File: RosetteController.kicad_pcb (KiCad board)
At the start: 4 copper layers, 100 x 50 mm, 10 parts

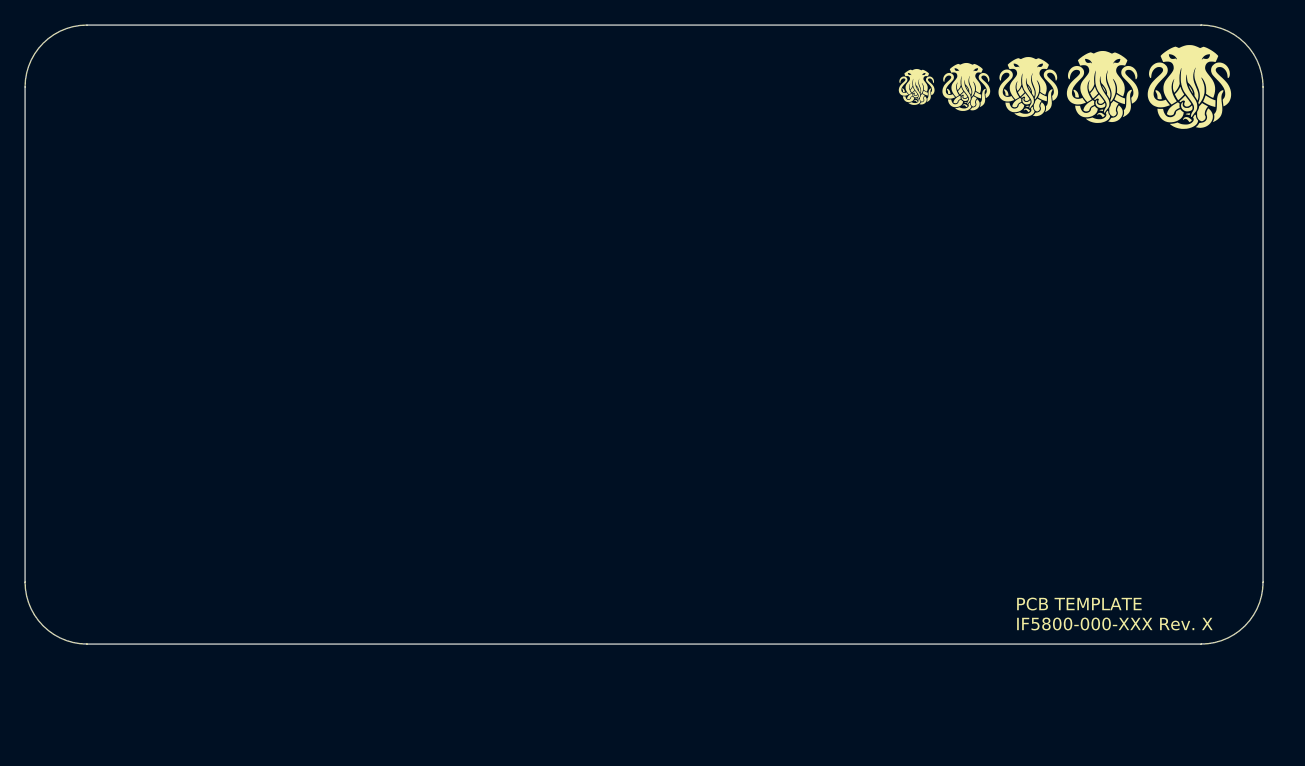
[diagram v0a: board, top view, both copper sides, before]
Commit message: Increased capacitance on motor driver
Increased capacitance on motor driver from 4.7uF to 44uF based on evaluation board testing.
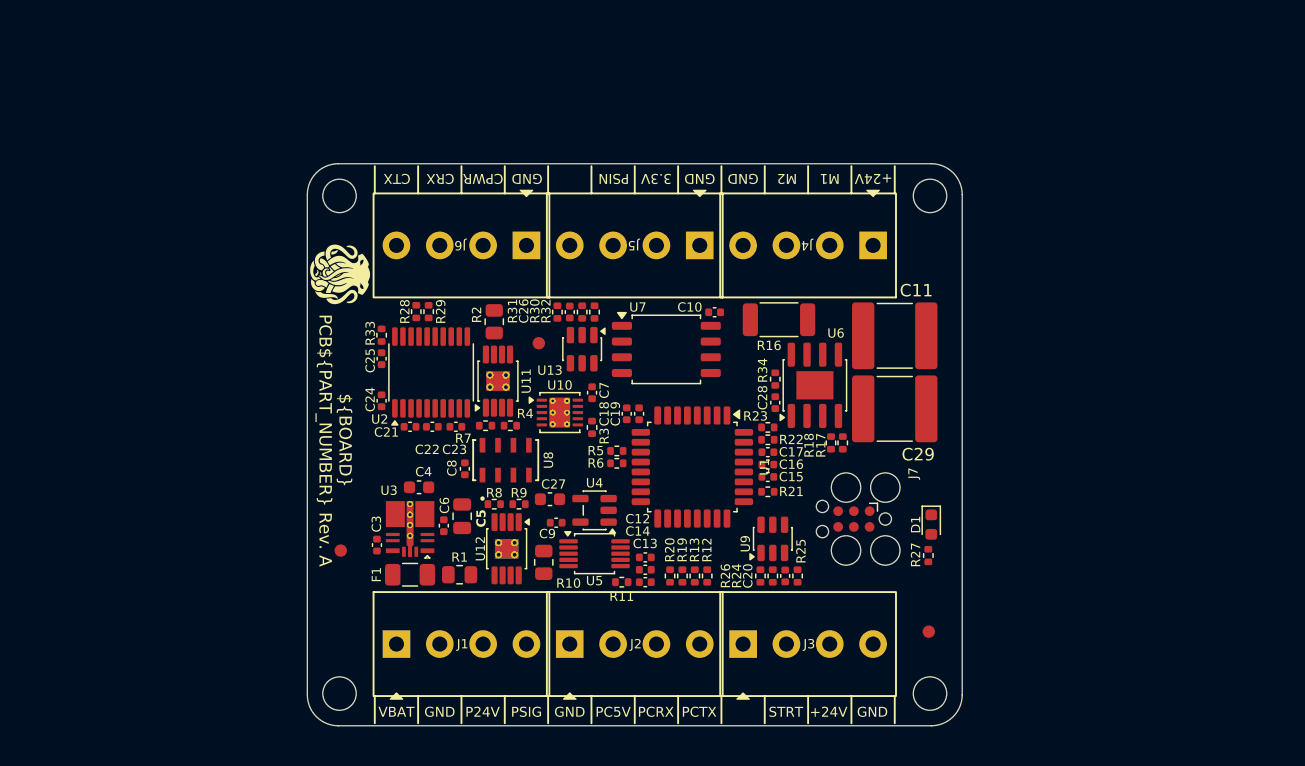
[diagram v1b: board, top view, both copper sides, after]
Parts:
- removed the G*** at (222.0, 105.0)
- removed the G*** at (174.0, 144.0)
- removed the G*** at (237.0, 105.0)
- removed the G*** at (226.0, 105.0)
- removed the G*** at (244.0, 105.0)
- removed the G*** at (169.0, 144.0)
- removed the G*** at (163.0, 144.0)
- removed the G*** at (178.0, 144.0)
- removed the G*** at (156.0, 144.0)
- added ?: , , F.Cu at (191.5, 125.7)
- added ?: , , F.Cu at (175.5, 142.4)
- added ?: Fiducial_1mm_Mask3mm, Fiducial:Fiducial_1mm_Mask3mm, F.Cu at (223.0, 149.0)
- added C10: 100nF, Capacitor_SMD:C_0402_1005Metric, F.Cu at (205.7, 123.2)
- added C11: 22uF, Capacitor_SMD:C_2220_5750Metric, F.Cu at (220.2, 125.1)
- added C12: 100nF, Capacitor_SMD:C_0402_1005Metric, F.Cu at (200.1, 143.0)
- added C13: 1uF, Capacitor_SMD:C_0402_1005Metric, F.Cu at (200.1, 145.0)
- added C14: 100nF, Capacitor_SMD:C_0402_1005Metric, F.Cu at (200.1, 144.0)
- added C15: 1uF, Capacitor_SMD:C_0402_1005Metric, F.Cu at (210.0, 136.5)
- added C16: 100nF, Capacitor_SMD:C_0402_1005Metric, F.Cu at (210.0, 135.5)
- added C17: 100nF, Capacitor_SMD:C_0402_1005Metric, F.Cu at (210.0, 134.5)
- added C18: 1uF, Capacitor_SMD:C_0402_1005Metric, F.Cu at (198.6, 131.4)
- added C19: 100nF, Capacitor_SMD:C_0402_1005Metric, F.Cu at (199.6, 131.4)
- added C20: 100nF, Capacitor_SMD:C_0402_1005Metric, F.Cu at (211.4, 144.5)
- added C21: 100nF, Capacitor_SMD:C_0402_1005Metric, F.Cu at (181.1, 132.4)
- added C22: 100nF, Capacitor_SMD:C_0402_1005Metric, F.Cu at (182.9, 132.4)
- added C23: 100nF, Capacitor_SMD:C_0402_1005Metric, F.Cu at (184.8, 132.4)
- added C24: 100nF, Capacitor_SMD:C_0402_1005Metric, F.Cu at (178.8, 130.3)
- added C25: 100nF, Capacitor_SMD:C_0402_1005Metric, F.Cu at (178.8, 126.9)
- added C26: 100nF, Capacitor_SMD:C_0402_1005Metric, F.Cu at (194.0, 123.2)
- added C27: 22uF, Capacitor_SMD:C_0603_1608Metric, F.Cu at (192.4, 138.3)
- added C28: 100nF, Capacitor_SMD:C_0402_1005Metric, F.Cu at (210.6, 130.5)
- added C29: 22uF, Capacitor_SMD:C_2220_5750Metric, F.Cu at (220.2, 131.0)
- added C3: 1uF, Capacitor_SMD:C_0402_1005Metric, F.Cu at (178.4, 142.0)
- added C4: 22uF, Capacitor_SMD:C_0603_1608Metric, F.Cu at (181.8, 137.3)
- added C5: 4.7uF, Capacitor_SMD:C_0805_2012Metric, F.Cu at (185.3, 139.7)
- added C6: 100nF, Capacitor_SMD:C_0402_1005Metric, F.Cu at (183.8, 140.4)
- added C7: 100nF, Capacitor_SMD:C_0402_1005Metric, F.Cu at (195.8, 129.7)
- added C8: 100nF, Capacitor_SMD:C_0402_1005Metric, F.Cu at (185.5, 135.8)
- added C9: 1uF, Capacitor_SMD:C_0402_1005Metric, F.Cu at (192.9, 140.2)
- added D1: LTST-C191KRKT, LED_SMD:LED_0603_1608Metric, F.Cu at (223.2, 140.3)
- added F1: 5A, Fuse:Fuse_1206_3216Metric, F.Cu at (181.1, 144.4)
- added J1: 284391-4, prj-footprints:CONN4_284391-4_TEC, F.Cu at (180.0, 150.0)
- added J2: 284391-4, prj-footprints:CONN4_284391-4_TEC, F.Cu at (194.0, 150.0)
- added J3: 284391-4, prj-footprints:CONN4_284391-4_TEC, F.Cu at (208.0, 150.0)
- added J4: 284391-4, prj-footprints:CONN4_284391-4_TEC, F.Cu at (218.5, 117.8)
- added J5: 284391-4, prj-footprints:CONN4_284391-4_TEC, F.Cu at (204.5, 117.8)
- added J6: 284391-4, prj-footprints:CONN4_284391-4_TEC, F.Cu at (190.5, 117.8)
- added J7: Conn_ARM_SWD_TagConnect_TC2030, Connector:Tag-Connect_TC2030-IDC-FP_2x03_P1.27mm_Vertical, F.Cu at (216.9, 139.9)
- added R1: 10m, Resistor_SMD:R_0805_2012Metric, F.Cu at (185.1, 144.4)
- added R10: 120, Resistor_SMD:R_0805_2012Metric, F.Cu at (191.9, 143.4)
- added R11: 0, Resistor_SMD:R_0402_1005Metric, F.Cu at (198.2, 145.0)
- added R12: 1k, Resistor_SMD:R_0402_1005Metric, F.Cu at (205.1, 144.5)
- added R13: 1k, Resistor_SMD:R_0402_1005Metric, F.Cu at (204.1, 144.5)
- added R16: 100m, Resistor_SMD:R_2010_5025Metric, F.Cu at (210.9, 123.8)
- added R17: 10k, Resistor_SMD:R_0402_1005Metric, F.Cu at (216.1, 133.8)
- added R18: 10k, Resistor_SMD:R_0402_1005Metric, F.Cu at (215.1, 133.8)
- added R19: 10k, Resistor_SMD:R_0402_1005Metric, F.Cu at (203.1, 144.5)
- added R2: 10m, Resistor_SMD:R_0805_2012Metric, F.Cu at (187.9, 124.0)
- added R20: 5k, Resistor_SMD:R_0402_1005Metric, F.Cu at (202.1, 144.5)
- added R21: 10k, Resistor_SMD:R_0402_1005Metric, F.Cu at (210.0, 137.7)
- added R22: 10k, Resistor_SMD:R_0402_1005Metric, F.Cu at (210.0, 133.5)
- added R23: 10k, Resistor_SMD:R_0402_1005Metric, F.Cu at (210.0, 132.5)
- added R24: 100k, Resistor_SMD:R_0402_1005Metric, F.Cu at (210.4, 144.5)
- added R25: 10k, Resistor_SMD:R_0402_1005Metric, F.Cu at (212.4, 144.5)
- added R26: 10k, Resistor_SMD:R_0402_1005Metric, F.Cu at (209.4, 144.5)
- added R27: 330, Resistor_SMD:R_0402_1005Metric, F.Cu at (223.0, 142.8)
- added R28: 330, Resistor_SMD:R_0402_1005Metric, F.Cu at (181.6, 123.1)
- added R29: 330, Resistor_SMD:R_0402_1005Metric, F.Cu at (182.6, 123.1)
- added R3: 10k, Resistor_SMD:R_0402_1005Metric, F.Cu at (195.8, 132.5)
- added R30: 10k, Resistor_SMD:R_0402_1005Metric, F.Cu at (195.0, 123.2)
- added R31: 10k, Resistor_SMD:R_0402_1005Metric, F.Cu at (193.0, 123.2)
- added R32: 10k, Resistor_SMD:R_0402_1005Metric, F.Cu at (196.0, 123.2)
- added R33: 100k, Resistor_SMD:R_0402_1005Metric, F.Cu at (178.8, 125.0)
- added R34: 10k, Resistor_SMD:R_0402_1005Metric, F.Cu at (210.6, 128.6)
- added R4: 1k, Resistor_SMD:R_0402_1005Metric, F.Cu at (189.2, 132.4)
- added R5: 10k, Resistor_SMD:R_0402_1005Metric, F.Cu at (197.8, 134.4)
- added R6: 10k, Resistor_SMD:R_0402_1005Metric, F.Cu at (197.8, 135.4)
- added R7: 10k, Resistor_SMD:R_0402_1005Metric, F.Cu at (187.2, 132.4)
- added R8: 1k, Resistor_SMD:R_0402_1005Metric, F.Cu at (187.9, 138.7)
- added R9: 10k, Resistor_SMD:R_0402_1005Metric, F.Cu at (189.9, 138.7)
- added REF**: MountingHole_2.7mm_M2.5_ISO14580, MountingHole:MountingHole_2.7mm_M2.5_ISO14580, F.Cu at (175.4, 154.0)
- added REF**: MountingHole_2.7mm_M2.5_ISO14580, MountingHole:MountingHole_2.7mm_M2.5_ISO14580, F.Cu at (175.4, 113.8)
- added REF**: MountingHole_2.7mm_M2.5_ISO14580, MountingHole:MountingHole_2.7mm_M2.5_ISO14580, F.Cu at (223.1, 154.0)
- added REF**: MountingHole_2.7mm_M2.5_ISO14580, MountingHole:MountingHole_2.7mm_M2.5_ISO14580, F.Cu at (223.1, 113.8)
- added U1: PIC32CM1216MC00032, Package_QFP:TQFP-32_7x7mm_P0.8mm, F.Cu at (203.9, 135.7)
- added U10: PAC1720, Package_DFN_QFN:DFN-10-1EP_3x3mm_P0.5mm_EP1.65x2.38mm_ThermalVias, F.Cu at (193.2, 131.3)
- added U11: TPS1H000, Package_SO:HVSSOP-8-1EP_3x3mm_P0.65mm_EP1.57x1.89mm_ThermalVias, F.Cu at (188.2, 128.8)
- added U12: TPS1H000, Package_SO:HVSSOP-8-1EP_3x3mm_P0.65mm_EP1.57x1.89mm_ThermalVias, F.Cu at (188.9, 142.3)
- added U13: TLV6713, Package_TO_SOT_SMD:TSOT-23-6, F.Cu at (195.0, 126.2)
- added U2: MAX3222EIPWR, Package_SO:Texas_PW0020A_TSSOP-20_4.4x6.5mm_P0.65mm, F.Cu at (182.8, 128.1)
- added U3: TPSM33610S3Q, Inkfish_IC:U_QFN-FCMOD_RDN0011B_TEX, F.Cu at (181.1, 140.5)
- added U4: LM4132AMF-2.0, Package_TO_SOT_SMD:SOT-23-5, F.Cu at (196.0, 139.2)
- added U5: MAX11201, Package_SO:MSOP-10_3x3mm_P0.5mm, F.Cu at (196.0, 142.7)
- added U6: TB67H450AFNG, Package_SO:SOIC-8-1EP_3.9x4.9mm_P1.27mm_EP2.29x3mm, F.Cu at (213.8, 129.1)
- added U7: MX25L25645G, Package_SO:SOIC-8_5.3x5.3mm_P1.27mm, F.Cu at (201.8, 126.2)
- added U8: MS860702BA01-50, Inkfish_Sensor:MS860702BA01-50_TEC, F.Cu at (188.8, 135.1)
- added U9: TLV6713, Package_TO_SOT_SMD:TSOT-23-6, F.Cu at (210.4, 141.5)
- moved G*** 57.6 mm to (175.4, 120.1), turned to -90 degrees
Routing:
- added copper zone on In2.Cu, net +3.3V
- added copper zone on In1.Cu, net GND
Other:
- board size 100 x 50 mm -> 52.9 x 45.4 mm
- board text added: "${BOARD} PCB${PART_NUMBER} Rev. ${REVISION}"
- board text added: "+24V"
- board text added: "3.3V"
- board text added: "CPWR"
- board text added: "CRX"
- board text added: "CTX"
- board text added: "GND"
- board text added: "M1"
- board text added: "M2"
- board text added: "P24V"
- board text added: "PC5V"
- board text added: "PCRX"
- board text added: "PCTX"
- board text added: "PSIG"
- board text added: "PSIN"
- board text added: "STRT"
- board text added: "VBAT"
- board text removed: "PCB TEMPLATE IF5800-000-XXX Rev. X"

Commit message: Layout Complete
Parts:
- removed ? (x2): , 
- removed J5, J6: 284391-4, prj-footprints:CONN4_284391-4_TEC
- removed R13: 1k, Resistor_SMD:R_0402_1005Metric
- added D2: PMEG60T50ELPX, Diode_SMD:D_SOD-128, F.Cu at (184.2, 140.3)
- added FID2: Fiducial_1mm_Mask3mm, Fiducial:Fiducial_1mm_Mask3mm, F.Cu at (172.3, 143.0)
- added FID3: Fiducial_1mm_Mask3mm, Fiducial:Fiducial_1mm_Mask3mm, F.Cu at (200.0, 127.0)
- added R35: 330, Resistor_SMD:R_0402_1005Metric, F.Cu at (193.3, 138.1)
- added R36: 330, Resistor_SMD:R_0402_1005Metric, F.Cu at (194.3, 138.1)
- added R37: DNP, Resistor_SMD:R_0402_1005Metric, F.Cu at (182.2, 144.0)
- added REF**: MountingHole_2.7mm_M2.5, MountingHole:MountingHole_2.7mm_M2.5, F.Cu at (172.3, 118.0)
- J1: value 284391-4 -> 0395016004; footprint prj-footprints:CONN4_284391-4_TEC -> Connector_Phoenix_MC:PhoenixContact_MCV_1,5_4-G-3.5_1x04_P3.50mm_Vertical
- J2: value 284391-4 -> 0395016008; footprint prj-footprints:CONN4_284391-4_TEC -> Connector_Phoenix_MC:PhoenixContact_MCV_1,5_8-G-3.5_1x08_P3.50mm_Vertical
- J3: value 284391-4 -> 0395016005; footprint prj-footprints:CONN4_284391-4_TEC -> Connector_Phoenix_MC:PhoenixContact_MCV_1,5_5-G-3.5_1x05_P3.50mm_Vertical
- J4: value 284391-4 -> 0395016006; footprint prj-footprints:CONN4_284391-4_TEC -> Connector_Phoenix_MC:PhoenixContact_MCV_1,5_6-G-3.5_1x06_P3.50mm_Vertical
- J7: footprint Connector:Tag-Connect_TC2030-IDC-FP_2x03_P1.27mm_Vertical -> Connector:Tag-Connect_TC2030-IDC-NL_2x03_P1.27mm_Vertical
- R12: value 1k -> 0
- REF** (x4): value MountingHole_2.7mm_M2.5_ISO14580 -> MountingHole_2.7mm_M2.5; footprint MountingHole:MountingHole_2.7mm_M2.5_ISO14580 -> MountingHole:MountingHole_2.7mm_M2.5
- moved REF** 55.0 mm to (172.3, 135.0)
- moved G*** 50.3 mm to (225.6, 125.0), turned to 90 degrees
- moved REF** 50.1 mm to (225.3, 118.0)
- moved J3 33.5 mm to (217.4, 117.9), turned to 180 degrees
- moved R12 23.0 mm to (182.2, 142.1), turned to -90 degrees
- moved J4 21.0 mm to (197.5, 117.9)
- moved C10 19.2 mm to (214.5, 140.3), turned to 90 degrees
- moved C7 16.7 mm to (179.7, 134.3), turned to -90 degrees
- moved R3 16.1 mm to (179.7, 131.5), turned to -90 degrees
- moved U7 15.0 mm to (211.1, 137.9), turned to -90 degrees
- moved R23 12.6 mm to (206.4, 144.6), turned to 90 degrees
- moved R21 12.2 mm to (199.9, 144.6), turned to 90 degrees
- moved R22 11.9 mm to (205.5, 144.6), turned to 90 degrees
- moved C17 11.4 mm to (204.6, 144.6), turned to -90 degrees
- moved R7 11.1 mm to (196.8, 126.7), turned to 90 degrees
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- gave numbers to parts that had none: 1
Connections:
- F1 pad 2: Net-(U10-SENSE1+) -> Net-(D2-A)
- J1 pad 1: /VBATT+ -> GND
- J1 pad 2: GND -> /VBATT+
- J2 pad 3: /FTDI_RX -> /RS232_RX
- J2 pad 4: /FTDI_TX -> /RS232_TX
- J3 pad 1: unconnected-(J3-Pin_1-Pad1) -> GND
- J3 pad 2: /START_PLUG -> /MOTOR1
- J3 pad 3: +24V -> /MOTOR2
- J3 pad 4: GND -> +3.3V
- J4 pad 1: +24V -> GND
- J4 pad 2: /MOTOR1 -> /CTD_PWR
- J4 pad 3: /MOTOR2 -> /CTD_RX
- J4 pad 4: GND -> /CTD_TX
- R1 pad 1: Net-(U10-SENSE1+) -> Net-(D2-K)
- R12 pad 1: /FTDI_TX -> +3.3V
- R12 pad 2: /PC_TXD -> Net-(U3-FB)
- U1 pad 1: /PRES_ON -> /RUN_WAKE
- U1 pad 14: /PAC_ALERT -> /HALL_SENSOR
- U1 pad 19: /HALL_SENSOR -> /PAC_ALERT
- U1 pad 20: /RUN_WAKE -> /RS232_SHDN
- U1 pad 23: /LED -> /PRES_ON
- U1 pad 4: /RS232_SHDN -> /LED
- U10 pad 1: Net-(U10-SENSE1+) -> Net-(D2-K)
- U2 pad 10: unconnected-(U2-ROUT2-Pad10) -> /PC_RXD
- U2 pad 12: GND -> /PC_TXD
- U2 pad 8: unconnected-(U2-DOUT2-Pad8) -> Net-(U2-DOUT2)
- U2 pad 9: GND -> Net-(U2-RIN2)
- U3 pad 9: +3.3V -> Net-(U3-FB)
- U6 pad 9: (no net) -> GND
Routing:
- net GND: track 0.00 -> 72.1 mm, vias 0 -> 69
- net +24V: track 0.00 -> 44.0 mm, vias 0 -> 21
- net /SDA: track 0.00 -> 41.7 mm, vias 0 -> 2
- net /SCL: track 0.00 -> 40.1 mm, vias 0 -> 2
- net +3.3V: track 0.00 -> 36.6 mm, vias 0 -> 25
- net /PAC_ALERT: track 0.00 -> 28.2 mm, vias 0 -> 2
- net /RS232_TX: track 0.00 -> 25.2 mm, vias 0 -> 2
- net /RS232_SHDN: track 0.00 -> 22.9 mm, vias 0 -> 2
- net /CTD_PWR: track 0.00 -> 20.7 mm
- net /CTD_ON: track 0.00 -> 20.4 mm
- net /RS232_RX: track 0.00 -> 19.7 mm, vias 0 -> 2
- net /RESET: track 0.00 -> 17.9 mm, vias 0 -> 2
- net /MOTOR_IN1: track 0.00 -> 15.7 mm, vias 0 -> 2
- net /MOTOR_IN2: track 0.00 -> 15.3 mm, vias 0 -> 2
- net /HALL_SENSOR: track 0.00 -> 14.8 mm
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- added copper zone on B.Cu, net +24V
- added copper zone on F.Cu, net +24V
- added copper zone on F.Cu, net +3.3V
- added copper zone on F.Cu, net /MOTOR1
- added copper zone on F.Cu, net /MOTOR2
- added copper zone on F.Cu, net GND
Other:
- board size 52.9 x 45.4 mm -> 59.7 x 45.6 mm
- board text added: "+3V3"
- board text added: "CTD PWR"
- board text added: "CTD RXD"
- board text added: "CTD TXD"
- board text added: "PC 5V"
- board text added: "PC RXD"
- board text added: "PC TXD"
- board text added: "PRES +24V"
- board text added: "PRES SIG"
- board text added: "PULS IN"
- board text added: "STATUS"
- board text added: "VBAT +"
- board text added: "VBAT -"
- board text removed: "3.3V"
- board text removed: "CPWR"
- board text removed: "CRX"
- board text removed: "CTX"
- board text removed: "P24V"
- board text removed: "PC5V"
- board text removed: "PCRX"
- board text removed: "PCTX"
- board text removed: "PSIG"
- board text removed: "PSIN"
- board text removed: "VBAT"

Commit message: Ready for preproduction checking
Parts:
- renumbered C20 to C1, C9 to C10, C27 to C11, C10 to C12, C6 to C13, C5 to C14, C21 to C15, C22 to C16, C23 to C17, C24 to C18, C7 to C19, C13 to C2, C19 to C20, C18 to C21, C25 to C22, C29 to C23, C28 to C24, C8 to C25, C11 to C26, C26 to C27, C14 to C3, C3 to C4, C12 to C5, C15 to C6, C16 to C7, C17 to C8, C4 to C9, D2 to D1, D1 to D2, G*** to G1, J7 to J5, REF** to M1, REF** to M2, REF** to M3, REF** to M4, REF** to M5, R26 to R1, R23 to R10, R37 to R11, R8 to R13, R9 to R14, R1 to R15, R27 to R16, R35 to R17, R36 to R18, R18 to R19, R24 to R2, R17 to R20, R6 to R21, R5 to R22, R3 to R23, R33 to R24, R34 to R25, R28 to R26, R29 to R27, R7 to R28, R2 to R29, R25 to R3, R4 to R30, R16 to R31, R30 to R32, R31 to R33, R32 to R34, R11 to R4, R10 to R5, R21 to R6, R20 to R7, R19 to R8, R22 to R9, U5 to U1, U6 to U10, U8 to U11, U13 to U12, U11 to U13, U12 to U2, U9 to U3, U3 to U4, U4 to U5, U1 to U6, U2 to U8, U10 to U9
